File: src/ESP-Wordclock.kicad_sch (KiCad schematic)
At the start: 1 part, among them J101 Conn_01x08_Pin

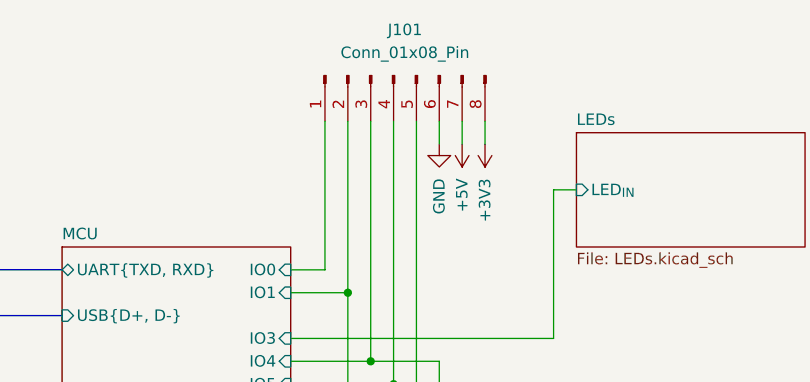
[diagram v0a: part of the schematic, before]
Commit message: Add: JLCPCB Database and selected components for the assembly
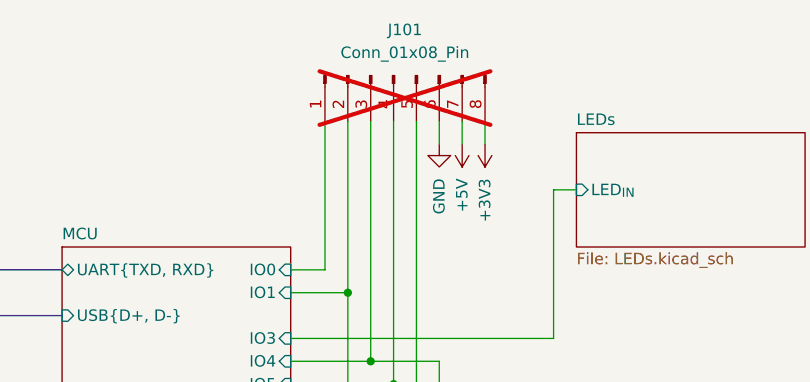
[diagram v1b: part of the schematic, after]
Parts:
- J101: now not fitted
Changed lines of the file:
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@@
 	(title_block
 		(title "Wordclock - Top")
-		(date "2024-11-01")
+		(date "2024-11-17")
 		(rev "A")
 		(company "ElektroNik Zoller")
@@
 		(in_bom yes)
 		(on_board yes)
-		(dnp no)
+		(dnp yes)
 		(fields_autoplaced yes)
 		(property "Reference" "J101"
@@
 			(at 163.83 38.1 0)
 			(effects
+				(font
+					(size 1.27 1.27)
+				)
+				(hide yes)
+			)
+		)
+		(property "Internal 1 Part no." ""
+			(at 163.83 38.1 0)
+			(effects
+				(font
+					(size 1.27 1.27)
+				)
+				(hide yes)
+			)
+		)
+		(property "Internal 2 Part no." ""
+			(at 163.83 38.1 0)
+			(effects
+				(font
+					(size 1.27 1.27)
+				)
+				(hide yes)
+			)
+		)
+		(property "Comment" ""
+			(at 163.83 38.1 0)
+			(effects
